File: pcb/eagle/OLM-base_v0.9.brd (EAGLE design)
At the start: 94.7 x 56.5 mm, 33 parts, among them IC1 ATMEGA, IC2 MCP1702-33, IC3 ENC28J60SP, J1 MAGJACK, J2 POWER_JACKPTH, X1 16 MHz, X3 25MHz

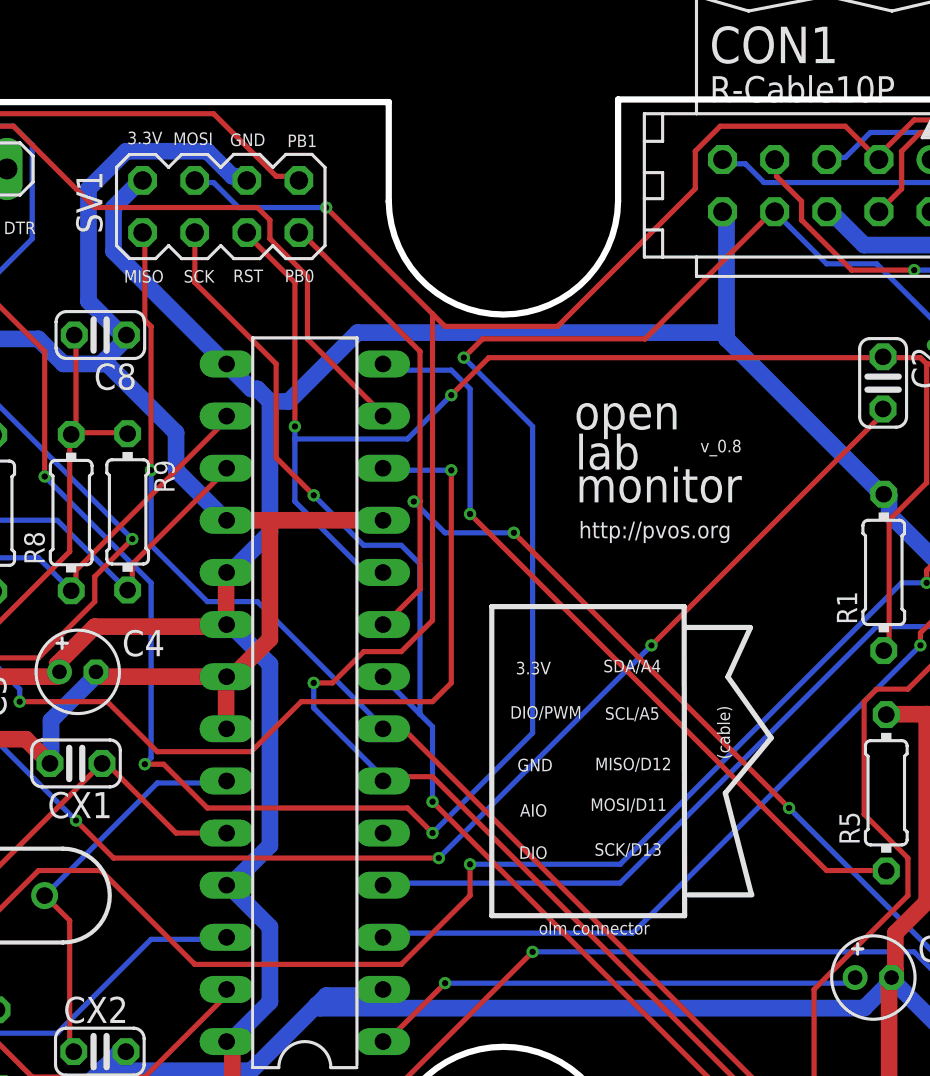
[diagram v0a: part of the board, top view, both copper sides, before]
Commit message: changed schematic
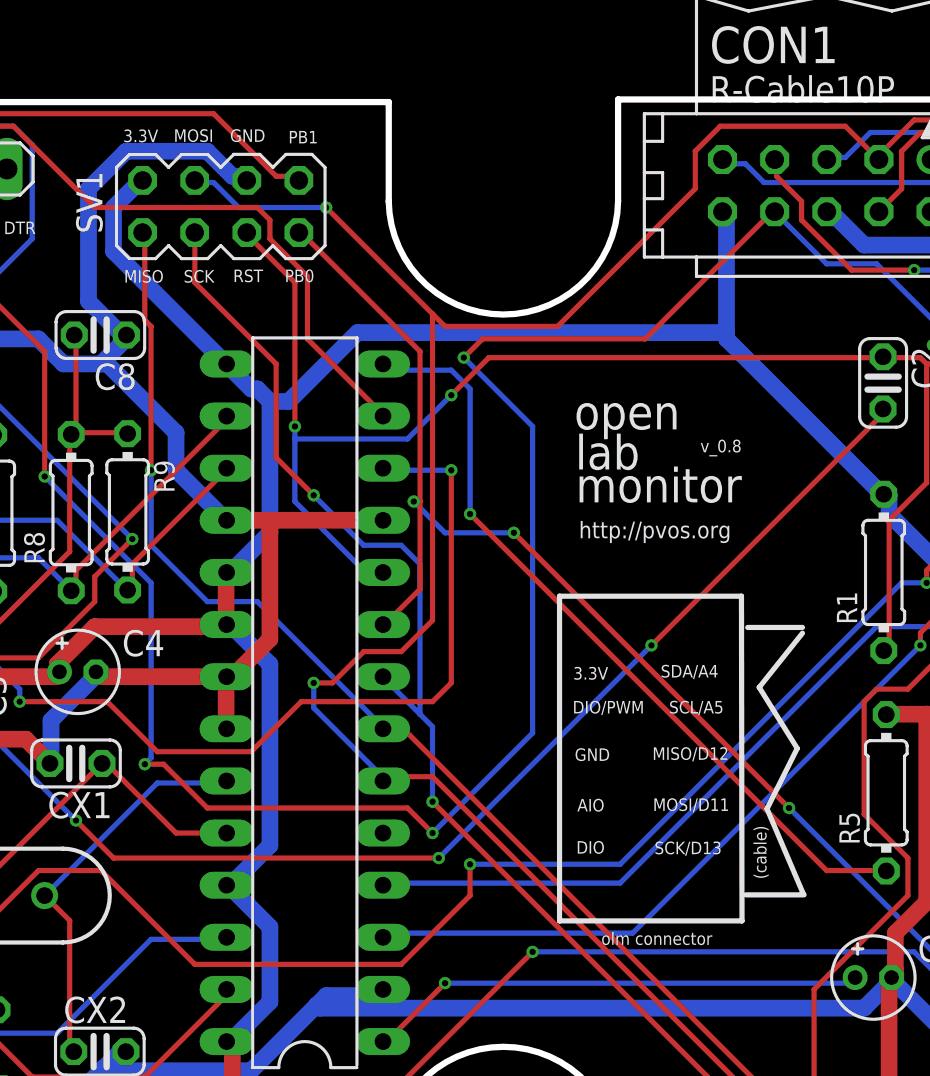
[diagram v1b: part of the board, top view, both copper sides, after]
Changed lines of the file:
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@@
 <setting verticaltext="up"/>
 </settings>
-<grid distance="0.01" unitdist="inch" unit="inch" style="lines" multiple="1" display="no" altdistance="0.025" altunitdist="inch" altunit="inch"/>
+<grid distance="0.001" unitdist="inch" unit="inch" style="lines" multiple="1" display="no" altdistance="0.025" altunitdist="inch" altunit="inch"/>
 <layers>
 <layer number="1" name="Top" color="4" fill="1" visible="yes" active="yes"/>
@@
 <hole x="88.7476" y="4.52881875" drill="3.2"/>
 <hole x="5.9436" y="4.52881875" drill="3.2"/>
-<wire x1="46.77918125" y1="16.697959375" x2="56.17718125" y2="16.697959375" width="0.254" layer="21"/>
-<wire x1="56.17718125" y1="16.697959375" x2="56.15178125" y2="31.760159375" width="0.254" layer="21"/>
-<wire x1="56.15178125" y1="31.760159375" x2="46.77918125" y2="31.760159375" width="0.254" layer="21"/>
-<wire x1="46.77918125" y1="31.760159375" x2="46.77918125" y2="16.697959375" width="0.254" layer="21"/>
-<text x="51.78298125" y="19.618959375" size="0.6096" layer="21">SCK/D13</text>
-<text x="51.57978125" y="21.803359375" size="0.6096" layer="21">MOSI/D11</text>
-<text x="51.80838125" y="23.784559375" size="0.6096" layer="21">MISO/D12</text>
-<text x="52.29098125" y="26.248359375" size="0.6096" layer="21">SCL/A5</text>
-<text x="52.21478125" y="28.559759375" size="0.6096" layer="21">SDA/A4</text>
-<text x="48.15078125" y="21.523959375" size="0.6096" layer="21">AIO</text>
-<text x="48.02378125" y="23.733759375" size="0.6096" layer="21">GND</text>
-<text x="47.66818125" y="26.299159375" size="0.6096" layer="21">DIO/PWM</text>
-<text x="47.94758125" y="28.458159375" size="0.6096" layer="21">3.3V</text>
-<text x="48.09998125" y="19.466559375" size="0.6096" layer="21">DIO</text>
-<wire x1="56.38038125" y1="17.713959375" x2="59.45378125" y2="17.713959375" width="0.254" layer="21"/>
-<wire x1="59.42838125" y1="17.739359375" x2="58.15838125" y2="22.666959375" width="0.254" layer="21"/>
-<wire x1="58.15838125" y1="22.666959375" x2="60.39358125" y2="25.359359375" width="0.254" layer="21"/>
-<wire x1="60.39358125" y1="25.359359375" x2="58.28538125" y2="28.331159375" width="0.254" layer="21"/>
-<wire x1="58.28538125" y1="28.331159375" x2="59.37758125" y2="30.718759375" width="0.254" layer="21"/>
-<wire x1="59.37758125" y1="30.744159375" x2="56.20258125" y2="30.744159375" width="0.254" layer="21"/>
-<text x="58.38698125" y="24.317959375" size="0.6096" layer="21" rot="R90">(cable)</text>
-<text x="49.06518125" y="15.783559375" size="0.6096" layer="21">olm connector</text>
+<wire x1="50.08118125" y1="16.443959375" x2="58.97118125" y2="16.443959375" width="0.254" layer="21"/>
+<wire x1="58.97118125" y1="16.443959375" x2="58.94578125" y2="32.268159375" width="0.254" layer="21"/>
+<wire x1="58.94578125" y1="32.268159375" x2="50.08118125" y2="32.268159375" width="0.254" layer="21"/>
+<wire x1="50.08118125" y1="32.268159375" x2="50.08118125" y2="16.443959375" width="0.254" layer="21"/>
+<text x="54.70398125" y="19.695159375" size="0.6096" layer="21">SCK/D13</text>
+<text x="54.62778125" y="21.803359375" size="0.6096" layer="21">MOSI/D11</text>
+<text x="54.60238125" y="24.292559375" size="0.6096" layer="21">MISO/D12</text>
+<text x="55.41518125" y="26.553159375" size="0.6096" layer="21">SCL/A5</text>
+<text x="55.00878125" y="28.305759375" size="0.6096" layer="21">SDA/A4</text>
+<text x="50.94478125" y="21.777959375" size="0.6096" layer="21">AIO</text>
+<text x="50.81778125" y="24.241759375" size="0.6096" layer="21">GND</text>
+<text x="50.71618125" y="26.553159375" size="0.6096" layer="21">DIO/PWM</text>
+<text x="50.74158125" y="28.204159375" size="0.6096" layer="21">3.3V</text>
+<text x="50.89398125" y="19.720559375" size="0.6096" layer="21">DIO</text>
+<wire x1="59.17438125" y1="17.713959375" x2="61.99378125" y2="17.713959375" width="0.254" layer="21"/>
+<wire x1="61.96838125" y1="17.739359375" x2="60.19038125" y2="21.904959375" width="0.254" layer="21"/>
+<wire x1="60.19038125" y1="21.904959375" x2="61.66358125" y2="24.851359375" width="0.254" layer="21"/>
+<wire x1="61.66358125" y1="24.851359375" x2="59.80938125" y2="27.823159375" width="0.254" layer="21"/>
+<wire x1="59.80938125" y1="27.823159375" x2="61.91758125" y2="30.464759375" width="0.254" layer="21"/>
+<wire x1="61.91758125" y1="30.744159375" x2="59.25058125" y2="30.744159375" width="0.254" layer="21"/>
+<text x="60.16498125" y="18.475959375" size="0.6096" layer="21" rot="R90">(cable)</text>
+<text x="52.11318125" y="15.275559375" size="0.6096" layer="21">olm connector</text>
 <text x="50.79238125" y="40.396159375" size="1.6764" layer="21">open</text>
 <text x="50.84318125" y="38.440359375" size="1.6764" layer="21">lab</text>
@@
 <text x="22.997159375" y="49.911" size="0.6096" layer="21">DTR</text>
 <text x="34.173159375" y="47.5742" size="0.6096" layer="21">RST</text>
-<text x="29.016959375" y="54.2925" size="0.6096" layer="21">3.3V</text>
-<text x="34.020759375" y="54.2036" size="0.6096" layer="21">GND</text>
-<text x="36.814759375" y="54.1528" size="0.6096" layer="21">PB1</text>
+<text x="28.813759375" y="54.3941" size="0.6096" layer="21">3.3V</text>
+<text x="34.020759375" y="54.4068" size="0.6096" layer="21">GND</text>
+<text x="36.865559375" y="54.3306" size="0.6096" layer="21">PB1</text>
 <text x="33.258759375" y="48.1584" size="0.6096" layer="21" rot="R180">SCK</text>
 <text x="30.794959375" y="48.1584" size="0.6096" layer="21" rot="R180">MISO</text>
 <text x="38.135559375" y="48.1838" size="0.6096" layer="21" rot="R180">PB0</text>
-<text x="31.252159375" y="54.2544" size="0.6096" layer="21">MOSI</text>
+<text x="31.277559375" y="54.4068" size="0.6096" layer="21">MOSI</text>
 </plain>
 <attributes>

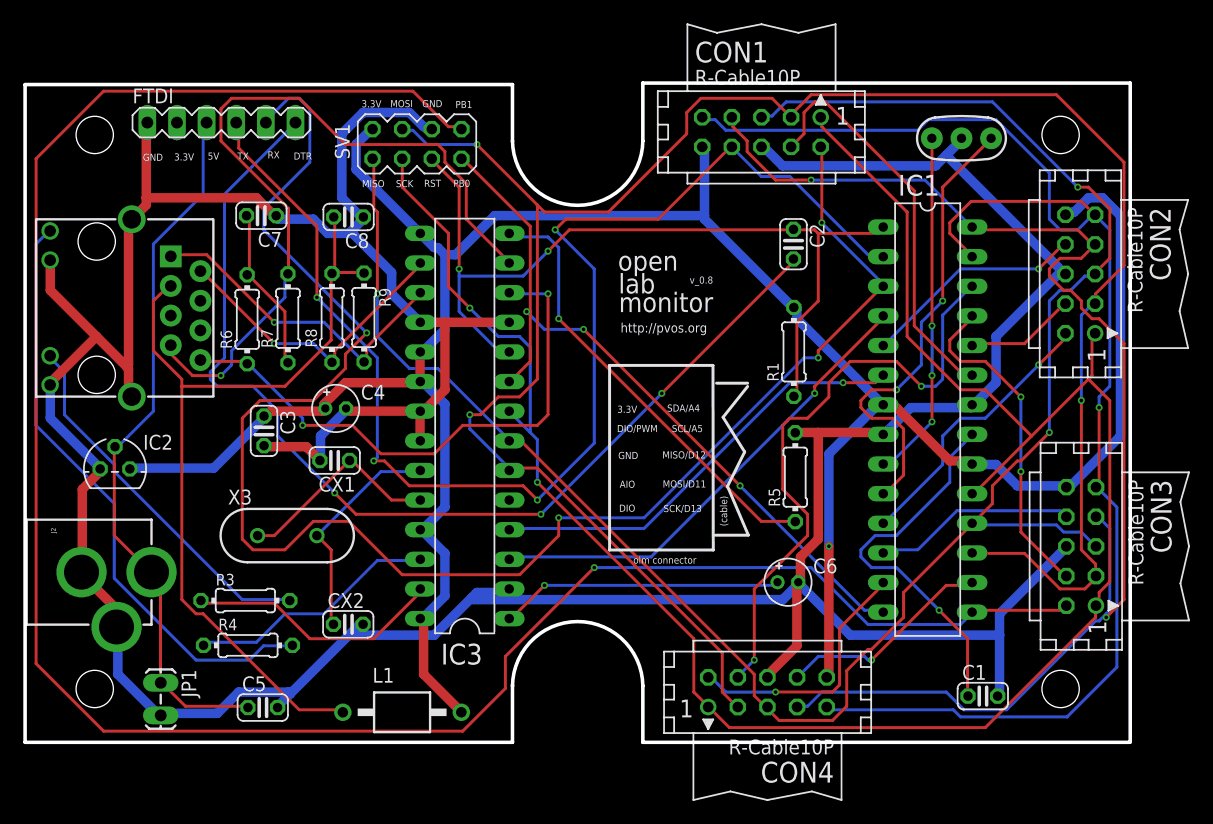
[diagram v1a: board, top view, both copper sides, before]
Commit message: flipped ic3
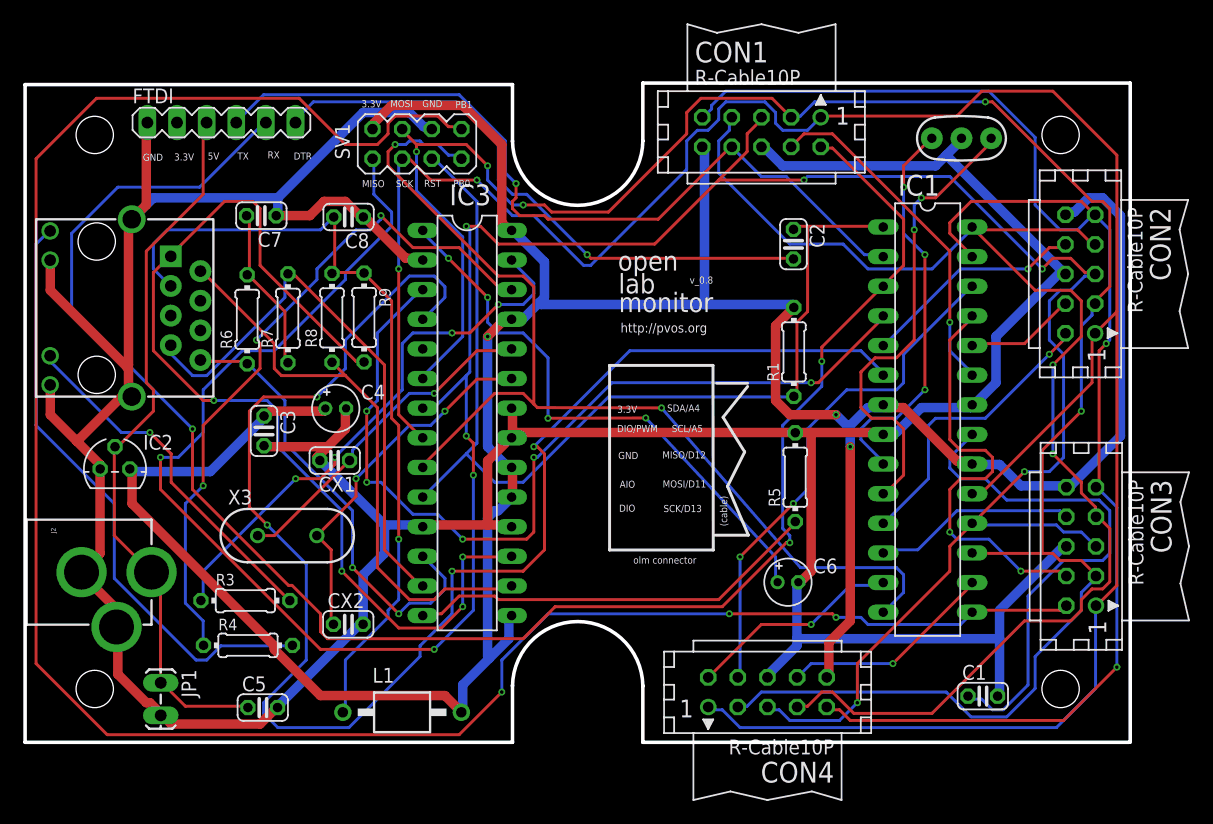
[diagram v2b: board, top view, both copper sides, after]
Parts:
- moved IC3 0.33 mm to (37.9, 27.3), turned to 270 degrees
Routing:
- net D4: track 37.5 -> 133.7 mm, vias 1 -> 4
- net MISO/D12: track 169.9 -> 248.7 mm, vias 3 -> 9
- net TD+: track 28.5 -> 86.3 mm, vias 1 -> 4
- net VCC: track 216.6 -> 260.3 mm, vias 1 -> 3
- net D0/RX: track 111.2 -> 70.7 mm, vias 4 -> 1
- net N$20: track 90.3 -> 51.0 mm, vias 3 -> 1
- net N$39: track 21.7 -> 59.2 mm, vias 0 -> 3
- net D2: track 41.1 -> 76.6 mm, vias 1 -> 5
- net SCK/D13: track 175.3 -> 206.1 mm
- net PB0/D8: track 64.0 -> 90.3 mm, vias 3 -> 2
- net N$37: track 22.1 -> 47.2 mm, vias 0 -> 4
- net N$50: track 24.3 -> 48.8 mm, vias 1 -> 4
- net TD-: track 26.2 -> 49.7 mm, vias 1 -> 0
- net RD+: track 66.8 -> 48.2 mm, vias 1 -> 0
- net RESET: track 73.3 -> 87.7 mm, vias 2 -> 0
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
